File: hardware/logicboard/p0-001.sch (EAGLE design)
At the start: 24 parts, among them IC1 74ALS05N, IC2 LTC485N, IC3 LTC485N, J0 DC5V, J1 DIN5, J2 DIN5, J3 DIN5, X1 NELTRON-7810-XPXC, X2 NELTRON-7810-XPXC

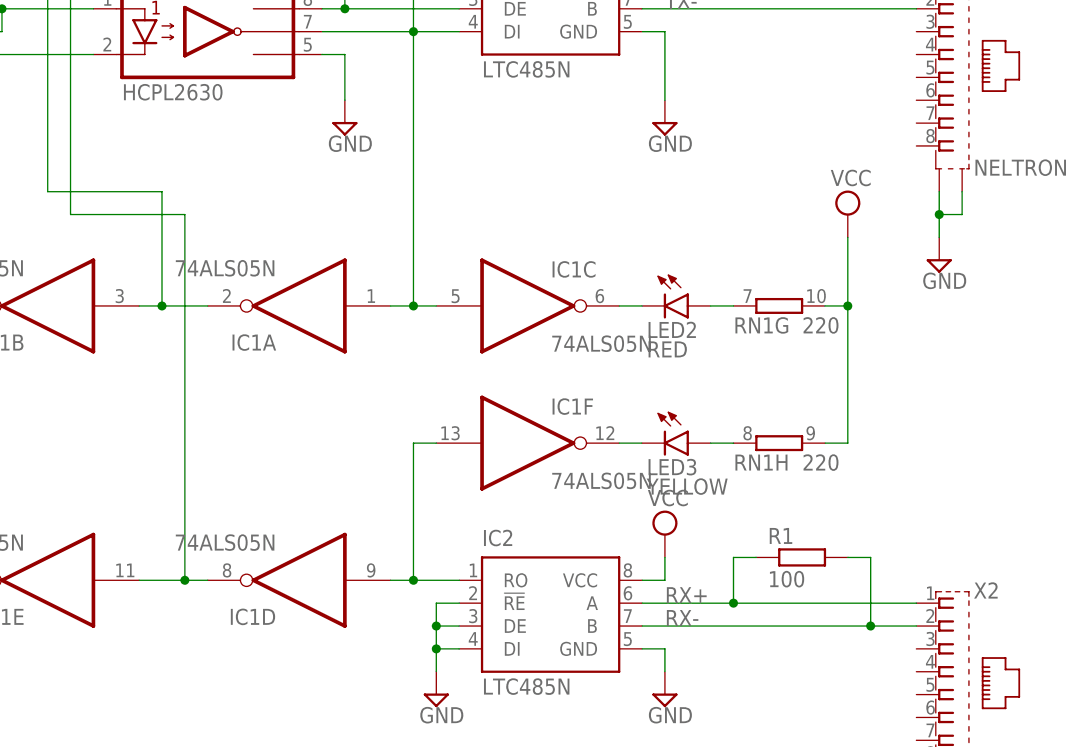
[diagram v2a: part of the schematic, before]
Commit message: Changed wiring of MIDI IN LED.
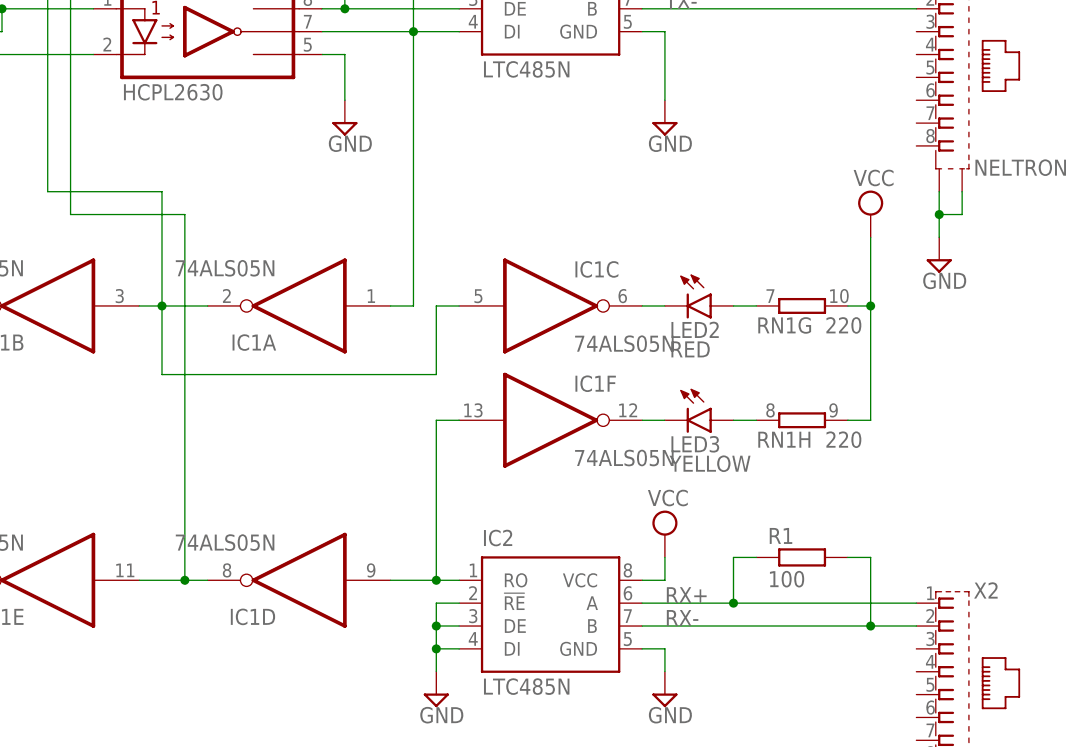
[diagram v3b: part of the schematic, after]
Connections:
- net NMIDITHRU: now also IC1C.I
- net TX: no longer IC1C.I
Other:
- moved on the sheet: IC1C, IC1F, LED2, LED3, RN1G, RN1H
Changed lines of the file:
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@@
 <attribute name="VALUE" x="73.66" y="99.06" size="1.778" layer="96" rot="R180"/>
 </instance>
-<instance part="IC1" gate="C" x="129.54" y="93.98" smashed="yes">
-<attribute name="NAME" x="132.08" y="97.155" size="1.778" layer="95"/>
-<attribute name="VALUE" x="132.08" y="88.9" size="1.778" layer="96"/>
+<instance part="IC1" gate="C" x="132.08" y="93.98" smashed="yes">
+<attribute name="NAME" x="134.62" y="97.155" size="1.778" layer="95"/>
+<attribute name="VALUE" x="134.62" y="88.9" size="1.778" layer="96"/>
 </instance>
 <instance part="IC1" gate="D" x="104.14" y="63.5" smashed="yes" rot="R180">
@@
 <attribute name="VALUE" x="73.66" y="68.58" size="1.778" layer="96" rot="R180"/>
 </instance>
-<instance part="IC1" gate="F" x="129.54" y="78.74" smashed="yes">
-<attribute name="NAME" x="132.08" y="81.915" size="1.778" layer="95"/>
-<attribute name="VALUE" x="132.08" y="73.66" size="1.778" layer="96"/>
+<instance part="IC1" gate="F" x="132.08" y="81.28" smashed="yes">
+<attribute name="NAME" x="134.62" y="84.455" size="1.778" layer="95"/>
+<attribute name="VALUE" x="134.62" y="76.2" size="1.778" layer="96"/>
 </instance>
 <instance part="SUPPLY19" gate="G$1" x="63.5" y="104.14" smashed="yes">
@@
 <attribute name="NAME" x="48.26" y="90.932" size="1.778" layer="95"/>
 </instance>
-<instance part="RN1" gate="G" x="157.48" y="93.98" smashed="yes">
-<attribute name="VALUE" x="160.02" y="90.932" size="1.778" layer="96"/>
-<attribute name="NAME" x="152.4" y="90.932" size="1.778" layer="95"/>
-</instance>
-<instance part="RN1" gate="H" x="157.48" y="78.74" smashed="yes">
-<attribute name="VALUE" x="160.02" y="75.692" size="1.778" layer="96"/>
-<attribute name="NAME" x="152.4" y="75.692" size="1.778" layer="95"/>
+<instance part="RN1" gate="G" x="160.02" y="93.98" smashed="yes">
+<attribute name="VALUE" x="162.56" y="90.932" size="1.778" layer="96"/>
+<attribute name="NAME" x="154.94" y="90.932" size="1.778" layer="95"/>
+</instance>
+<instance part="RN1" gate="H" x="160.02" y="81.28" smashed="yes">
+<attribute name="VALUE" x="162.56" y="78.232" size="1.778" layer="96"/>
+<attribute name="NAME" x="154.94" y="78.232" size="1.778" layer="95"/>
 </instance>
 <instance part="RN2" gate="1" x="71.12" y="157.48" smashed="yes" rot="R270">
@@
 <attribute name="VALUE" x="51.435" y="24.765" size="1.778" layer="96"/>
 </instance>
-<instance part="LED2" gate="G$1" x="147.32" y="93.98" smashed="yes" rot="R270">
-<attribute name="NAME" x="142.748" y="90.424" size="1.778" layer="95"/>
-<attribute name="VALUE" x="142.748" y="88.265" size="1.778" layer="96"/>
-</instance>
-<instance part="SUPPLY30" gate="G$1" x="165.1" y="104.14" smashed="yes">
-<attribute name="VALUE" x="163.195" y="107.315" size="1.778" layer="96"/>
-</instance>
-<instance part="LED3" gate="G$1" x="147.32" y="78.74" smashed="yes" rot="R270">
-<attribute name="NAME" x="142.748" y="75.184" size="1.778" layer="95"/>
-<attribute name="VALUE" x="142.748" y="73.025" size="1.778" layer="96"/>
+<instance part="LED2" gate="G$1" x="149.86" y="93.98" smashed="yes" rot="R270">
+<attribute name="NAME" x="145.288" y="90.424" size="1.778" layer="95"/>
+<attribute name="VALUE" x="145.288" y="88.265" size="1.778" layer="96"/>
+</instance>
+<instance part="SUPPLY30" gate="G$1" x="167.64" y="104.14" smashed="yes">
+<attribute name="VALUE" x="165.735" y="107.315" size="1.778" layer="96"/>
+</instance>
+<instance part="LED3" gate="G$1" x="149.86" y="81.28" smashed="yes" rot="R270">
+<attribute name="NAME" x="145.288" y="77.724" size="1.778" layer="95"/>
+<attribute name="VALUE" x="145.288" y="75.565" size="1.778" layer="96"/>
 </instance>
 <instance part="R1" gate="G$1" x="160.02" y="66.04" smashed="yes">
@@
 <segment>
 <pinref part="RN1" gate="G" pin="2"/>
-<wire x1="162.56" y1="93.98" x2="165.1" y2="93.98" width="0.1524" layer="91"/>
-<wire x1="165.1" y1="93.98" x2="165.1" y2="101.6" width="0.1524" layer="91"/>
+<wire x1="165.1" y1="93.98" x2="167.64" y2="93.98" width="0.1524" layer="91"/>
+<wire x1="167.64" y1="93.98" x2="167.64" y2="101.6" width="0.1524" layer="91"/>
 <pinref part="SUPPLY30" gate="G$1" pin="VCC"/>
-<wire x1="165.1" y1="93.98" x2="165.1" y2="78.74" width="0.1524" layer="91"/>
-<junction x="165.1" y="93.98"/>
+<wire x1="167.64" y1="93.98" x2="167.64" y2="81.28" width="0.1524" layer="91"/>
+<junction x="167.64" y="93.98"/>
 <pinref part="RN1" gate="H" pin="2"/>
-<wire x1="165.1" y1="78.74" x2="162.56" y2="78.74" width="0.1524" layer="91"/>
+<wire x1="167.64" y1="81.28" x2="165.1" y2="81.28" width="0.1524" layer="91"/>
 </segment>
 </net>
@@
 <segment>
 <pinref part="IC2" gate="G$1" pin="RO"/>
-<wire x1="121.92" y1="63.5" x2="116.84" y2="63.5" width="0.1524" layer="91"/>
 <pinref part="IC1" gate="D" pin="I"/>
+<wire x1="121.92" y1="63.5" x2="119.38" y2="63.5" width="0.1524" layer="91"/>
 <pinref part="IC1" gate="F" pin="I"/>
-<wire x1="116.84" y1="63.5" x2="114.3" y2="63.5" width="0.1524" layer="91"/>
-<wire x1="119.38" y1="78.74" x2="116.84" y2="78.74" width="0.1524" layer="91"/>
-<wire x1="116.84" y1="78.74" x2="116.84" y2="63.5" width="0.1524" layer="91"/>
-<junction x="116.84" y="63.5"/>
+<wire x1="119.38" y1="63.5" x2="114.3" y2="63.5" width="0.1524" layer="91"/>
+<wire x1="121.92" y1="81.28" x2="119.38" y2="81.28" width="0.1524" layer="91"/>
+<wire x1="119.38" y1="81.28" x2="119.38" y2="63.5" width="0.1524" layer="91"/>
+<junction x="119.38" y="63.5"/>
 </segment>
 </net>
@@
 <wire x1="116.84" y1="93.98" x2="116.84" y2="124.46" width="0.1524" layer="91"/>
 <junction x="116.84" y="124.46"/>
-<pinref part="IC1" gate="C" pin="I"/>
-<wire x1="119.38" y1="93.98" x2="116.84" y2="93.98" width="0.1524" layer="91"/>
-<junction x="116.84" y="93.98"/>
 <pinref part="RN2" gate="1" pin="2"/>
 <wire x1="71.12" y1="152.4" x2="116.84" y2="152.4" width="0.1524" layer="91"/>
@@
 <pinref part="RN2" gate="1" pin="3"/>
 <wire x1="71.12" y1="147.32" x2="76.2" y2="147.32" width="0.1524" layer="91"/>
+<pinref part="IC1" gate="C" pin="I"/>
+<wire x1="121.92" y1="93.98" x2="119.38" y2="93.98" width="0.1524" layer="91"/>
+<wire x1="119.38" y1="93.98" x2="119.38" y2="86.36" width="0.1524" layer="91"/>
+<wire x1="119.38" y1="86.36" x2="88.9" y2="86.36" width="0.1524" layer="91"/>
+<wire x1="88.9" y1="86.36" x2="88.9" y2="93.98" width="0.1524" layer="91"/>
 </segment>
 </net>
@@
 <pinref part="LED2" gate="G$1" pin="C"/>
 <pinref part="IC1" gate="C" pin="O"/>
-<wire x1="142.24" y1="93.98" x2="139.7" y2="93.98" width="0.1524" layer="91"/>
+<wire x1="144.78" y1="93.98" x2="142.24" y2="93.98" width="0.1524" layer="91"/>
 </segment>
 </net>
@@
 <pinref part="RN1" gate="G" pin="1"/>
 <pinref part="LED2" gate="G$1" pin="A"/>
-<wire x1="152.4" y1="93.98" x2="149.86" y2="93.98" width="0.1524" layer="91"/>
+<wire x1="154.94" y1="93.98" x2="152.4" y2="93.98" width="0.1524" layer="91"/>
 </segment>
 </net>
@@
 <pinref part="RN1" gate="H" pin="1"/>
 <pinref part="LED3" gate="G$1" pin="A"/>
-<wire x1="152.4" y1="78.74" x2="149.86" y2="78.74" width="0.1524" layer="91"/>
+<wire x1="154.94" y1="81.28" x2="152.4" y2="81.28" width="0.1524" layer="91"/>
 </segment>
 </net>
@@
 <pinref part="LED3" gate="G$1" pin="C"/>
 <pinref part="IC1" gate="F" pin="O"/>
-<wire x1="142.24" y1="78.74" x2="139.7" y2="78.74" width="0.1524" layer="91"/>
-</segment>
-</net>
+<wire x1="144.78" y1="81.28" x2="142.24" y2="81.28" width="0.1524" layer="91"/>
+</segment>
+</net>

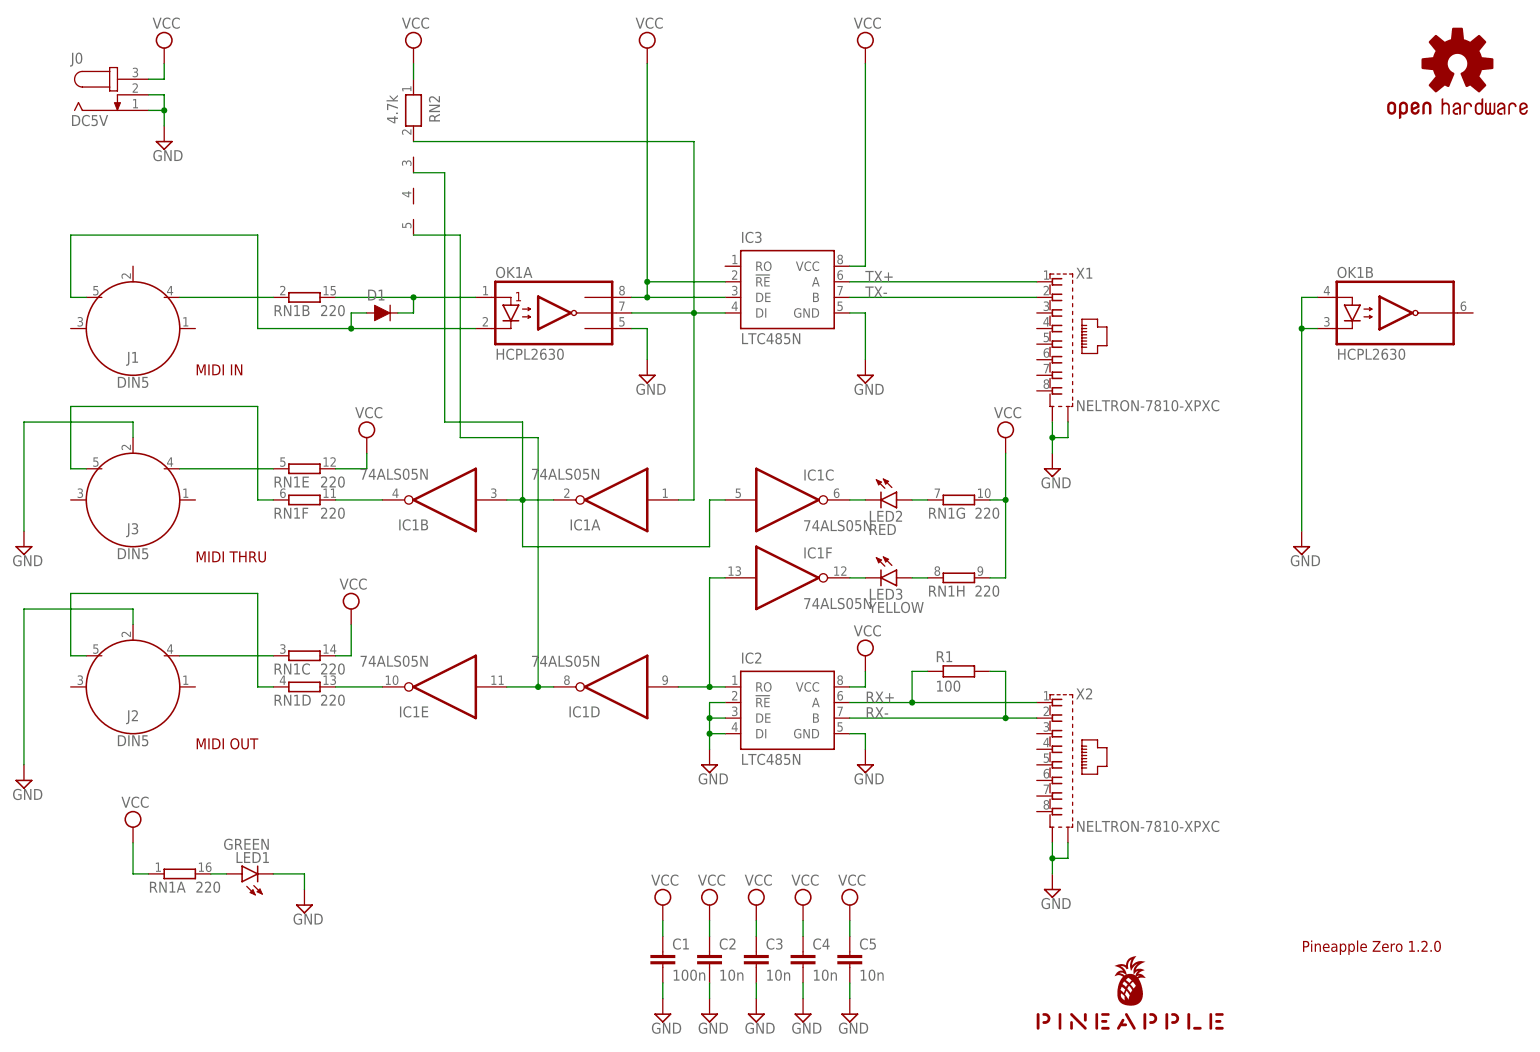
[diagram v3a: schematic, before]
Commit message: Changed Rs for LEDs.
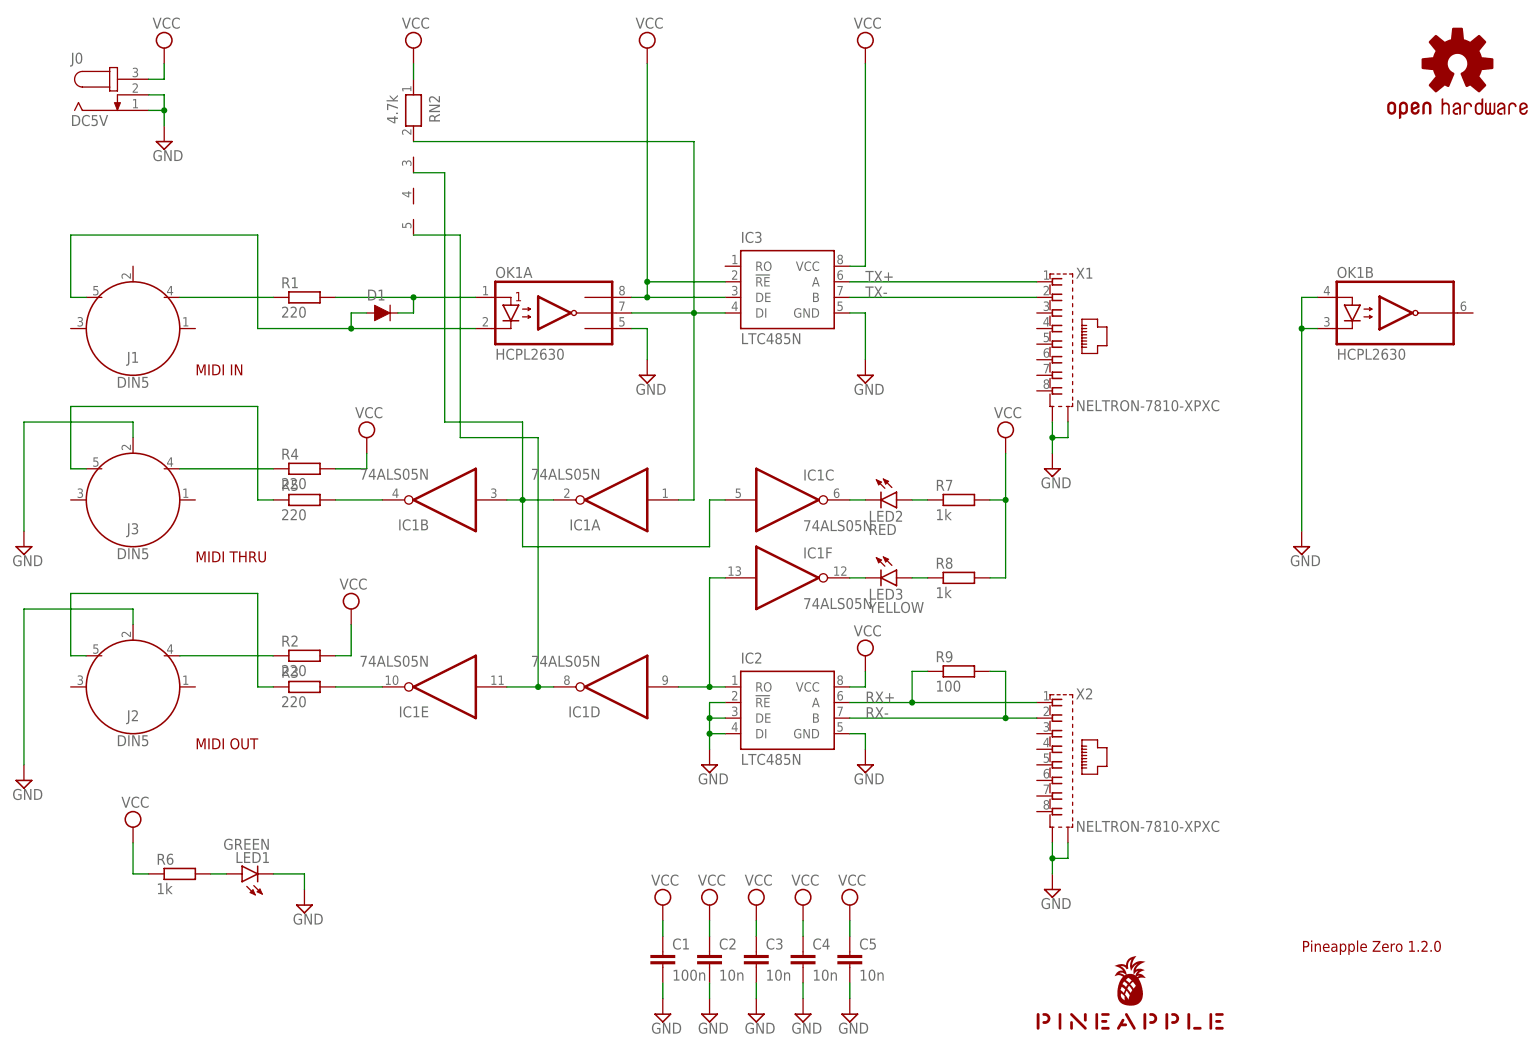
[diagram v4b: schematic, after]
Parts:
- removed RN1: 220, resistor-dil:8R-N
- added R2, R3, R4, R5: 220, rcl:R-EU_0204/5
- added R6, R7, R8: 1k, rcl:R-EU_0204/5
- added R9: 100, rcl:R-EU_0204/5
- R1: value 100 -> 220
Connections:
- net MIDIIN: now also R1.2; no longer RN1B.2
- net MIDIINLEDA: now also R7.1; no longer RN1G.1
- net MIDIOUT: now also R3.2; no longer RN1D.2
- net MIDITHRU: now also R5.2; no longer RN1F.2
- net MISND: now also R1.1; no longer RN1B.1
- net MORTN: now also R3.1; no longer RN1D.1
- net MOSND: now also R2.1; no longer RN1C.1
- net MTRTN: now also R5.1; no longer RN1F.1
- net MTSND: now also R4.1; no longer RN1E.1
- net PWRLED: now also R6.2; no longer RN1A.2
- net RX+: now also R9.1; no longer R1.1
- net RX-: now also R9.2; no longer R1.2
- net RXLEDA: now also R8.1; no longer RN1H.1
- net VCC: now also R2.2, R4.2, R6.1, R7.2, R8.2; no longer RN1A.1, RN1C.2, RN1E.2, RN1G.2, RN1H.2
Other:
- moved on the sheet: R1

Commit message: Added MIDI signal checker.
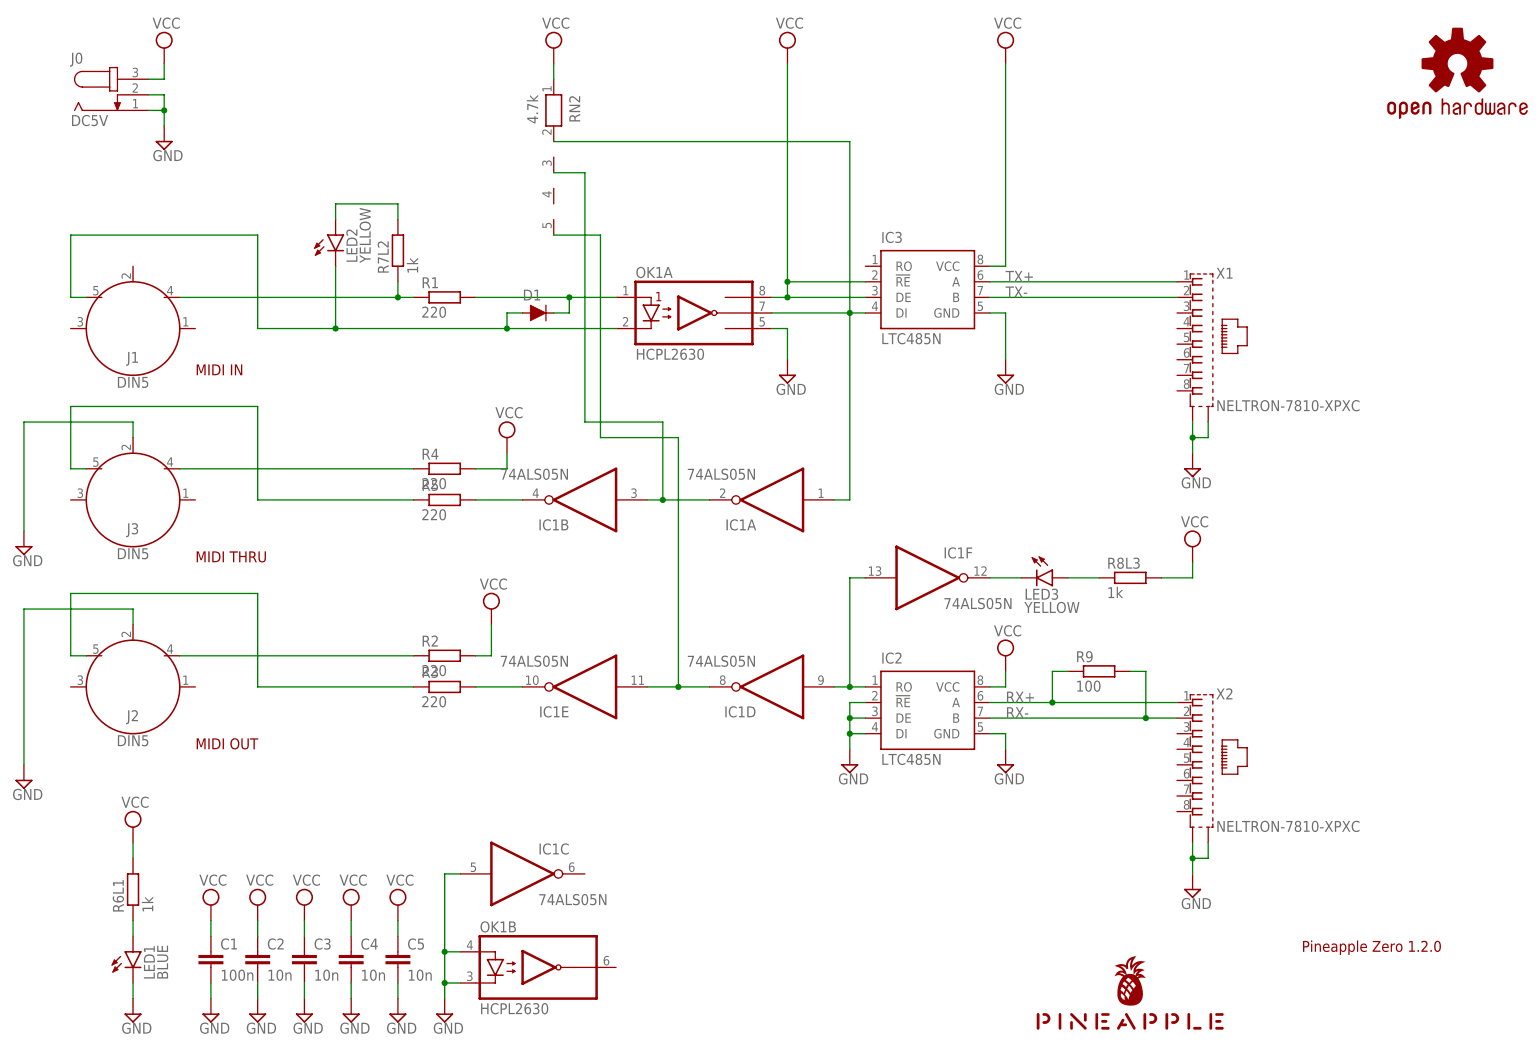
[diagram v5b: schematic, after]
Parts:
- removed R6, R7, R8: 1k, rcl:R-EU_0204/5
- added R6L1, R7L2, R8L3: 1k, rcl:R-EU_0204/5
- LED1: value GREEN -> BLUE
- LED2: value RED -> YELLOW
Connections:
- net RXLED renamed N$3
- removed net MIDIINLED: IC1C.O, LED2.C
- removed net MIDIINLEDA: LED2.A, R7.1
- removed net PWRLED: LED1.A, R6.2
- removed net RXLEDA: LED3.A, R8.1
- new net N$1: LED2.A, R7L2.2
- new net N$2: LED3.A, R8L3.1
- new net N$4: LED1.A, R6L1.1
- net GND: now also IC1C.I
- net MIRTN: now also LED2.C
- net MISND: now also R7L2.1
- net NMIDITHRU: no longer IC1C.I
- net VCC: now also R6L1.2, R8L3.2; no longer R6.1, R7.2, R8.2
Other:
- moved on the sheet: C1, C2, C3, C4, C5, D1, IC1A, IC1B, IC1C, IC1D, IC1E, IC1F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
